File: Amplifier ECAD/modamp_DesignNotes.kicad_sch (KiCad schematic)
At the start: 0 parts

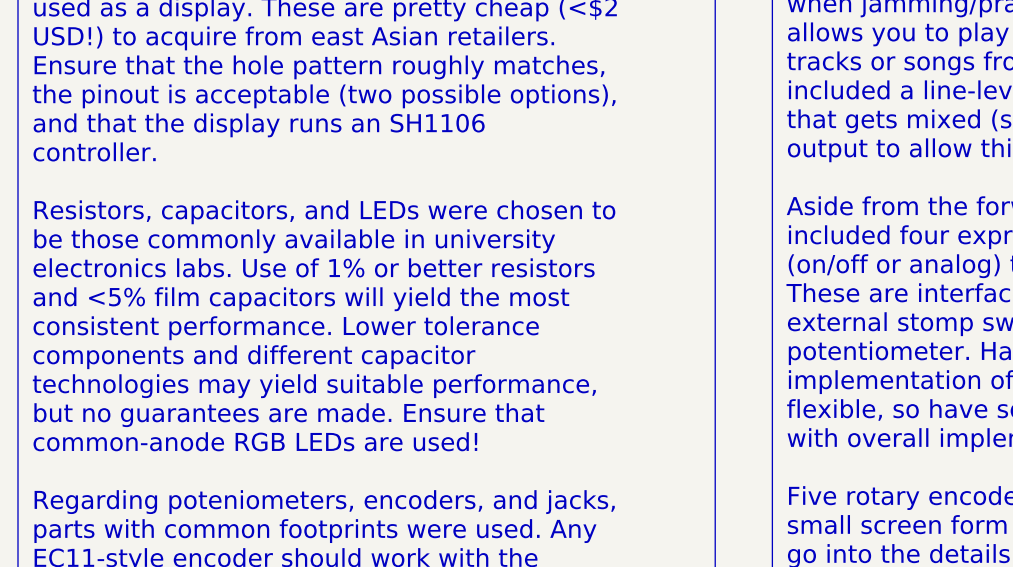
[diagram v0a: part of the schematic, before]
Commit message: File renaming; updating supplier references
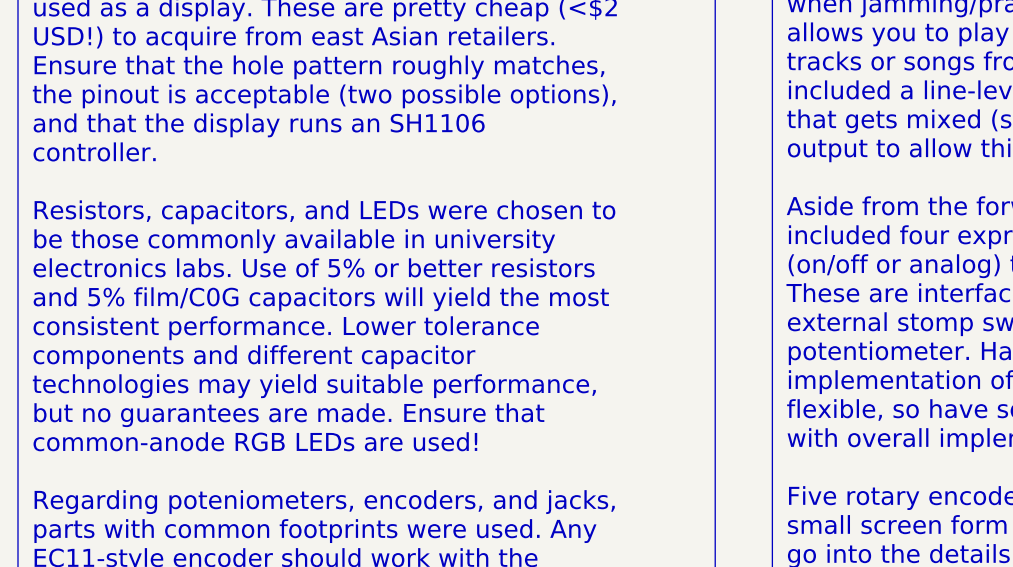
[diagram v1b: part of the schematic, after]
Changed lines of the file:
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@@
     (effects (font (size 2 2) (thickness 0.4) bold (color 132 0 0 1)) (justify left top))
   )
-  (text_box "\n\n\nI designed this amplifier to help teach the basics of digital signal processing. As a result, the design aims to be easy to assemble (read: through-hole components) and primarily constructed out of cheap, readily-available components.\n\nThe main active analog component used in the design was an MCP6004 quad op-amp. Generally, any kinda rail-to-rail input/output, >600kHz GBP, and <0.1% THD+N parts should do the trick here. Suitable replacements include the MCP6294, LMC6484, TLV2464, and TLV2474 among other more expensive options. \n\nThe Teensy 4.1 was chosen as the main DSP MCU due to its pretty decent computational power, relatively low cost, great community support, ease of firmware implementation, and use in other classes taught at MIT. \n\nI'm intending for a generic 1.3\" Monochrome OLED screen with an SH1106 controller to be used as a display. These are pretty cheap (<$2 USD!) to acquire from east Asian retailers. Ensure that the hole pattern roughly matches, the pinout is acceptable (two possible options), and that the display runs an SH1106 controller.\n\nResistors, capacitors, and LEDs were chosen to be those commonly available in university electronics labs. Use of 1% or better resistors and <5% film capacitors will yield the most consistent performance. Lower tolerance components and different capacitor technologies may yield suitable performance, but no guarantees are made. Ensure that common-anode RGB LEDs are used!\n\nRegarding poteniometers, encoders, and jacks, parts with common footprints were used. Any EC11-style encoder should work with the design, and are available cheaply from east Asian retailers. \"RV09-sytle\" potentiometers can be similarly sourced cheaply. The exact same thing can be said for \"PJ-307-style\" 3.5mm TRS jacks, and \"PJ-609-style\" 1/4\" TRS jacks.\n\n\n"
+  (text_box "\n\n\nI designed this amplifier to help teach the basics of digital signal processing. As a result, the design aims to be easy to assemble (read: through-hole components) and primarily constructed out of cheap, readily-available components.\n\nThe main active analog component used in the design was an MCP6004 quad op-amp. Generally, any kinda rail-to-rail input/output, >600kHz GBP, and <0.1% THD+N parts should do the trick here. Suitable replacements include the MCP6294, LMC6484, TLV2464, and TLV2474 among other more expensive options. \n\nThe Teensy 4.1 was chosen as the main DSP MCU due to its pretty decent computational power, relatively low cost, great community support, ease of firmware implementation, and use in other classes taught at MIT. \n\nI'm intending for a generic 1.3\" Monochrome OLED screen with an SH1106 controller to be used as a display. These are pretty cheap (<$2 USD!) to acquire from east Asian retailers. Ensure that the hole pattern roughly matches, the pinout is acceptable (two possible options), and that the display runs an SH1106 controller.\n\nResistors, capacitors, and LEDs were chosen to be those commonly available in university electronics labs. Use of 5% or better resistors and 5% film/C0G capacitors will yield the most consistent performance. Lower tolerance components and different capacitor technologies may yield suitable performance, but no guarantees are made. Ensure that common-anode RGB LEDs are used!\n\nRegarding poteniometers, encoders, and jacks, parts with common footprints were used. Any EC11-style encoder should work with the design, and are available cheaply from east Asian retailers. \"RV09-sytle\" potentiometers can be similarly sourced cheaply. The exact same thing can be said for \"PJ-307-style\" 3.5mm TRS jacks, and \"PJ-609-style\" 1/4\" TRS jacks.\n\n\n"
     (at 16.51 17.78 0) (size 77.47 173.99)
     (stroke (width 0) (type default) (color 200 175 200 1))
